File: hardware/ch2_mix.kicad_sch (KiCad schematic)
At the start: 6 parts, among them U24 TC4-19G2, U25 BAT-15-099R, U26 TC4-19G2

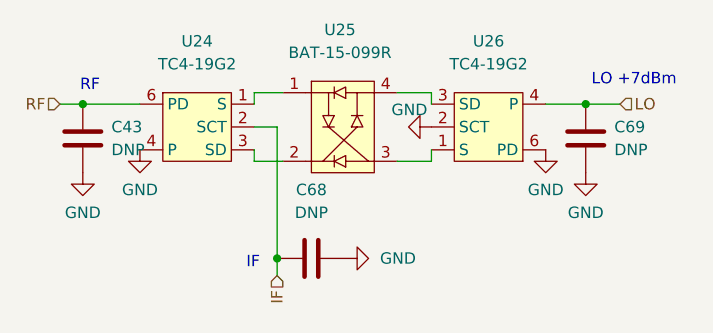
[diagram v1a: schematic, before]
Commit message: Update FEM hardware design for production version
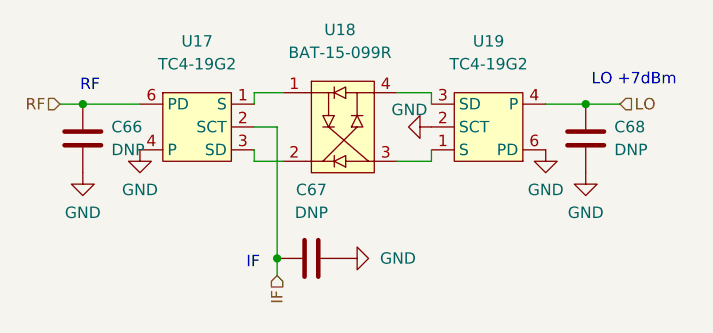
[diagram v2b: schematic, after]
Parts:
- renumbered C43 to C66, C68 to C67, C69 to C68, U24 to U17, U25 to U18, U26 to U19
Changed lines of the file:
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@@
   (symbol (lib_id "power:GND") (at 149.225 114.3 90) (unit 1)
     (in_bom yes) (on_board yes) (dnp no) (fields_autoplaced)
-    (property "Reference" "#PWR0147" (at 155.575 114.3 0)
+    (property "Reference" "#PWR0104" (at 155.575 114.3 0)
       (effects (font (size 1.27 1.27)) hide)
     )
@@
       (project "GreX Frontend"
         (path "/e63e39d7-6ac0-4ffd-8aa3-1841a4541b55/546148dc-8a5c-4178-ace4-1d6889891417/2f65e89e-e7a4-4405-8f8d-c41909a9666d"
-          (reference "#PWR0147") (unit 1)
+          (reference "#PWR0104") (unit 1)
         )
       )
@@
   (symbol (lib_id "power:GND") (at 171.45 102.235 0) (unit 1)
     (in_bom yes) (on_board yes) (dnp no) (fields_autoplaced)
-    (property "Reference" "#PWR0146" (at 171.45 108.585 0)
+    (property "Reference" "#PWR0106" (at 171.45 108.585 0)
       (effects (font (size 1.27 1.27)) hide)
     )
@@
       (project "GreX Frontend"
         (path "/e63e39d7-6ac0-4ffd-8aa3-1841a4541b55/546148dc-8a5c-4178-ace4-1d6889891417/2f65e89e-e7a4-4405-8f8d-c41909a9666d"
-          (reference "#PWR0146") (unit 1)
+          (reference "#PWR0106") (unit 1)
         )
       )
@@
   (symbol (lib_id "power:GND") (at 175.895 104.775 0) (unit 1)
     (in_bom yes) (on_board yes) (dnp no) (fields_autoplaced)
-    (property "Reference" "#PWR0145" (at 175.895 111.125 0)
+    (property "Reference" "#PWR0107" (at 175.895 111.125 0)
       (effects (font (size 1.27 1.27)) hide)
     )
@@
       (project "GreX Frontend"
         (path "/e63e39d7-6ac0-4ffd-8aa3-1841a4541b55/546148dc-8a5c-4178-ace4-1d6889891417/2f65e89e-e7a4-4405-8f8d-c41909a9666d"
-          (reference "#PWR0145") (unit 1)
+          (reference "#PWR0107") (unit 1)
         )
       )
@@
   (symbol (lib_id "RF Parts:TC4-19G2") (at 132.715 99.06 0) (unit 1)
     (in_bom yes) (on_board yes) (dnp no) (fields_autoplaced)
-    (property "Reference" "U24" (at 132.715 90.17 0)
+    (property "Reference" "U17" (at 132.715 90.17 0)
       (effects (font (size 1.27 1.27)))
     )
@@
       (project "GreX Frontend"
         (path "/e63e39d7-6ac0-4ffd-8aa3-1841a4541b55/546148dc-8a5c-4178-ace4-1d6889891417/2f65e89e-e7a4-4405-8f8d-c41909a9666d"
-          (reference "U24") (unit 1)
+          (reference "U17") (unit 1)
         )
       )
@@
   (symbol (lib_id "RF Parts:TC4-19G2") (at 165.1 100.33 180) (unit 1)
     (in_bom yes) (on_board yes) (dnp no) (fields_autoplaced)
-    (property "Reference" "U26" (at 165.1 90.17 0)
+    (property "Reference" "U19" (at 165.1 90.17 0)
       (effects (font (size 1.27 1.27)))
     )
@@
       (project "GreX Frontend"
         (path "/e63e39d7-6ac0-4ffd-8aa3-1841a4541b55/546148dc-8a5c-4178-ace4-1d6889891417/2f65e89e-e7a4-4405-8f8d-c41909a9666d"
-          (reference "U26") (unit 1)
+          (reference "U19") (unit 1)
         )
       )
@@
   (symbol (lib_id "Device:C") (at 175.895 100.965 0) (unit 1)
     (in_bom yes) (on_board yes) (dnp no) (fields_autoplaced)
-    (property "Reference" "C69" (at 179.07 99.6949 0)
+    (property "Reference" "C68" (at 179.07 99.6949 0)
       (effects (font (size 1.27 1.27)) (justify left))
     )
@@
       (project "GreX Frontend"
         (path "/e63e39d7-6ac0-4ffd-8aa3-1841a4541b55/546148dc-8a5c-4178-ace4-1d6889891417/2f65e89e-e7a4-4405-8f8d-c41909a9666d"
-          (reference "C69") (unit 1)
+          (reference "C68") (unit 1)
         )
       )
@@
   (symbol (lib_id "power:GND") (at 158.75 99.695 270) (unit 1)
     (in_bom yes) (on_board yes) (dnp no)
-    (property "Reference" "#PWR0149" (at 152.4 99.695 0)
+    (property "Reference" "#PWR0105" (at 152.4 99.695 0)
       (effects (font (size 1.27 1.27)) hide)
     )
@@
       (project "GreX Frontend"
         (path "/e63e39d7-6ac0-4ffd-8aa3-1841a4541b55/546148dc-8a5c-4178-ace4-1d6889891417/2f65e89e-e7a4-4405-8f8d-c41909a9666d"
-          (reference "#PWR0149") (unit 1)
+          (reference "#PWR0105") (unit 1)
         )
       )
@@
   (symbol (lib_id "power:GND") (at 126.365 102.235 0) (unit 1)
     (in_bom yes) (on_board yes) (dnp no) (fields_autoplaced)
-    (property "Reference" "#PWR0142" (at 126.365 108.585 0)
+    (property "Reference" "#PWR0103" (at 126.365 108.585 0)
       (effects (font (size 1.27 1.27)) hide)
     )
@@
       (project "GreX Frontend"
         (path "/e63e39d7-6ac0-4ffd-8aa3-1841a4541b55/546148dc-8a5c-4178-ace4-1d6889891417/2f65e89e-e7a4-4405-8f8d-c41909a9666d"
-          (reference "#PWR0142") (unit 1)
+          (reference "#PWR0103") (unit 1)
         )
       )
@@
   (symbol (lib_id "Device:C") (at 120.015 100.965 0) (unit 1)
     (in_bom yes) (on_board yes) (dnp no) (fields_autoplaced)
-    (property "Reference" "C43" (at 123.19 99.6949 0)
+    (property "Reference" "C66" (at 123.19 99.6949 0)
       (effects (font (size 1.27 1.27)) (justify left))
     )
@@
       (project "GreX Frontend"
         (path "/e63e39d7-6ac0-4ffd-8aa3-1841a4541b55/546148dc-8a5c-4178-ace4-1d6889891417/2f65e89e-e7a4-4405-8f8d-c41909a9666d"
-          (reference "C43") (unit 1)
+          (reference "C66") (unit 1)
         )
       )
@@
   (symbol (lib_id "RF Parts:BAT-15-099R") (at 148.59 99.06 0) (unit 1)
     (in_bom yes) (on_board yes) (dnp no) (fields_autoplaced)
-    (property "Reference" "U25" (at 148.59 88.9 0)
+    (property "Reference" "U18" (at 148.59 88.9 0)
       (effects (font (size 1.27 1.27)))
     )
@@
       (project "GreX Frontend"
         (path "/e63e39d7-6ac0-4ffd-8aa3-1841a4541b55/546148dc-8a5c-4178-ace4-1d6889891417/2f65e89e-e7a4-4405-8f8d-c41909a9666d"
-          (reference "U25") (unit 1)
+          (reference "U18") (unit 1)
         )
       )
@@
   (symbol (lib_id "power:GND") (at 120.015 104.775 0) (unit 1)
     (in_bom yes) (on_board yes) (dnp no) (fields_autoplaced)
-    (property "Reference" "#PWR0143" (at 120.015 111.125 0)
+    (property "Reference" "#PWR0102" (at 120.015 111.125 0)
       (effects (font (size 1.27 1.27)) hide)
     )
@@
       (project "GreX Frontend"
         (path "/e63e39d7-6ac0-4ffd-8aa3-1841a4541b55/546148dc-8a5c-4178-ace4-1d6889891417/2f65e89e-e7a4-4405-8f8d-c41909a9666d"
-          (reference "#PWR0143") (unit 1)
+          (reference "#PWR0102") (unit 1)
         )
       )
@@
   (symbol (lib_id "Device:C") (at 145.415 114.3 90) (unit 1)
     (in_bom yes) (on_board yes) (dnp no) (fields_autoplaced)
-    (property "Reference" "C68" (at 145.415 106.68 90)
+    (property "Reference" "C67" (at 145.415 106.68 90)
       (effects (font (size 1.27 1.27)))
     )
@@
       (project "GreX Frontend"
         (path "/e63e39d7-6ac0-4ffd-8aa3-1841a4541b55/546148dc-8a5c-4178-ace4-1d6889891417/2f65e89e-e7a4-4405-8f8d-c41909a9666d"
-          (reference "C68") (unit 1)
-        )
-      )
+          (reference "C67") (unit 1)
+        )
+      )
